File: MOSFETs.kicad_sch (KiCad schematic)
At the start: 45 parts, among them J10 Sol_1, J6 Sol_2, J7 Sol_3, J8 Sol_4, J9 Motor, Q2 IRF540N, Q3 IRF540N, Q4 IRF540N, Q5 IRF540N, Q6 IRF540N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

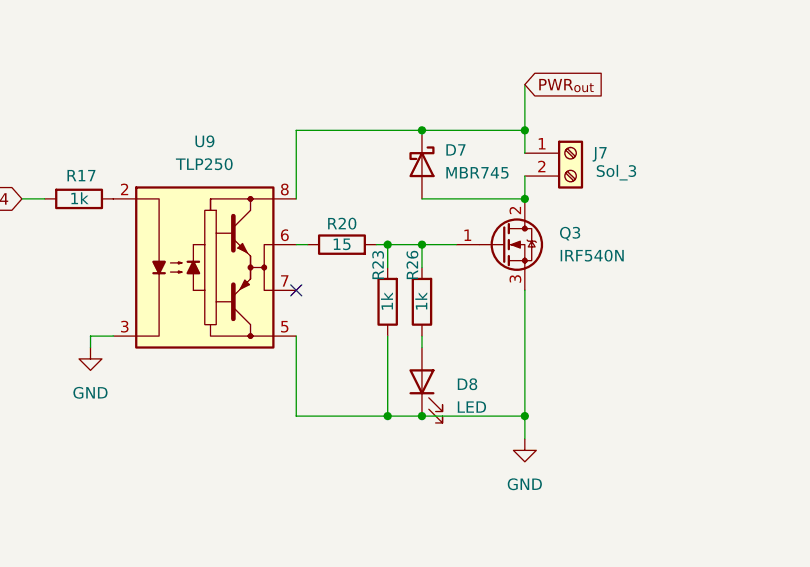
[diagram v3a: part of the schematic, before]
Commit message: feat: Battery charging Circuit is added.
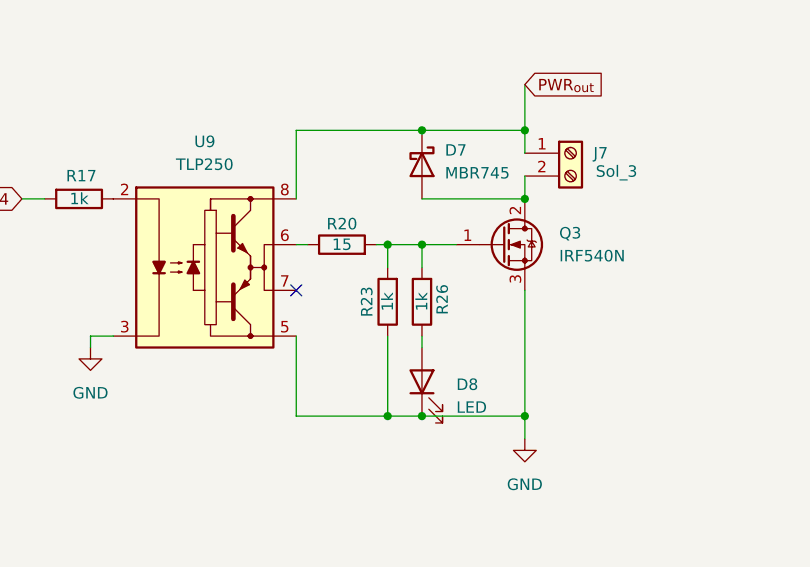
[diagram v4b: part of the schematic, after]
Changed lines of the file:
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@@
 		(dnp no)
 		(property "Reference" "R26"
-			(at 84.074 101.346 90)
+			(at 87.376 105.156 90)
 			(effects
 				(font
@@
 		(dnp no)
 		(property "Reference" "R23"
-			(at 80.264 101.346 90)
-			(effects
-				(font
+			(at 78.994 105.41 90)
+			(effects
+				(font
